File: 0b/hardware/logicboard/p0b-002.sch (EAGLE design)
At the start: 30 parts, among them IC1 7404D, IC4 LTC485S, IC5 LTC485S, J0 DC5V, J7 DIN5, J9 DIN5, X7 NELTRON-7810-XPXC

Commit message: Added Direct-5V resistor pattern.
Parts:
- added R0: Inf, rcl:R-EU_M2012
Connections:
- net V+: now also R0.1
- net VCC: now also R0.2
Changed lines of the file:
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@@
 <part name="S1" library="switch-dil" library_urn="urn:adsk.eagle:library:375" deviceset="DIP04YL" device="" package3d_urn="urn:adsk.eagle:package:27255/2" value="MIDIPHANTOM"/>
 <part name="SUPPLY9" library="supply2" library_urn="urn:adsk.eagle:library:372" deviceset="GND" device=""/>
+<part name="R0" library="rcl" library_urn="urn:adsk.eagle:library:334" deviceset="R-EU_" device="M2012" package3d_urn="urn:adsk.eagle:package:23561/2" value="Inf"/>
 </parts>
 <sheets>
@@
 <instance part="SUPPLY9" gate="GND" x="83.82" y="86.36" smashed="yes">
 <attribute name="VALUE" x="86.995" y="83.185" size="1.778" layer="96"/>
+</instance>
+<instance part="R0" gate="G$1" x="63.5" y="162.56" smashed="yes">
+<attribute name="NAME" x="59.69" y="164.0586" size="1.778" layer="95"/>
+<attribute name="VALUE" x="59.69" y="159.258" size="1.778" layer="96"/>
 </instance>
 </instances>
@@
 <wire x1="66.04" y1="154.94" x2="76.2" y2="154.94" width="0.1524" layer="91"/>
 <wire x1="76.2" y1="154.94" x2="76.2" y2="149.86" width="0.1524" layer="91"/>
+<pinref part="R0" gate="G$1" pin="2"/>
+<wire x1="68.58" y1="162.56" x2="76.2" y2="162.56" width="0.1524" layer="91"/>
+<wire x1="76.2" y1="162.56" x2="76.2" y2="154.94" width="0.1524" layer="91"/>
+<junction x="76.2" y="154.94"/>
 </segment>
 </net>
@@
 <label x="76.2" y="96.52" size="1.778" layer="95"/>
 <label x="76.2" y="91.44" size="1.778" layer="95"/>
-</segment>
-</net>
+<pinref part="R0" gate="G$1" pin="1"/>
+<wire x1="58.42" y1="162.56" x2="50.8" y2="162.56" width="0.1524" layer="91"/>
+<wire x1="50.8" y1="162.56" x2="50.8" y2="154.94" width="0.1524" layer="91"/>
+<junction x="50.8" y="154.94"/>
+</segment>
+</net>

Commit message: Pinhead.
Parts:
- removed R0: Inf, rcl:R-EU_M2012
- added JP1: (no value), pinhead:PINHD-1X2
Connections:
- net V+: now also JP1.1; no longer R0.1
- net VCC: now also JP1.2; no longer R0.2
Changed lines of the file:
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@@
 <part name="S1" library="switch-dil" library_urn="urn:adsk.eagle:library:375" deviceset="DIP04YL" device="" package3d_urn="urn:adsk.eagle:package:27255/2" value="MIDIPHANTOM"/>
 <part name="SUPPLY9" library="supply2" library_urn="urn:adsk.eagle:library:372" deviceset="GND" device=""/>
-<part name="R0" library="rcl" library_urn="urn:adsk.eagle:library:334" deviceset="R-EU_" device="M2012" package3d_urn="urn:adsk.eagle:package:23561/2" value="Inf"/>
+<part name="JP1" library="pinhead" library_urn="urn:adsk.eagle:library:325" deviceset="PINHD-1X2" device="" package3d_urn="urn:adsk.eagle:package:22435/2"/>
 </parts>
 <sheets>
@@
 <attribute name="VALUE" x="86.995" y="83.185" size="1.778" layer="96"/>
 </instance>
-<instance part="R0" gate="G$1" x="63.5" y="162.56" smashed="yes">
-<attribute name="NAME" x="59.69" y="164.0586" size="1.778" layer="95"/>
-<attribute name="VALUE" x="59.69" y="159.258" size="1.778" layer="96"/>
+<instance part="JP1" gate="G$1" x="63.5" y="165.1" smashed="yes" rot="R90">
+<attribute name="NAME" x="57.785" y="158.75" size="1.778" layer="95" rot="R90"/>
+<attribute name="VALUE" x="68.58" y="158.75" size="1.778" layer="96" rot="R90"/>
 </instance>
 </instances>
@@
 <wire x1="66.04" y1="154.94" x2="76.2" y2="154.94" width="0.1524" layer="91"/>
 <wire x1="76.2" y1="154.94" x2="76.2" y2="149.86" width="0.1524" layer="91"/>
-<pinref part="R0" gate="G$1" pin="2"/>
-<wire x1="68.58" y1="162.56" x2="76.2" y2="162.56" width="0.1524" layer="91"/>
-<wire x1="76.2" y1="162.56" x2="76.2" y2="154.94" width="0.1524" layer="91"/>
+<wire x1="76.2" y1="160.02" x2="76.2" y2="154.94" width="0.1524" layer="91"/>
 <junction x="76.2" y="154.94"/>
+<pinref part="JP1" gate="G$1" pin="2"/>
+<wire x1="63.5" y1="162.56" x2="63.5" y2="160.02" width="0.1524" layer="91"/>
+<wire x1="63.5" y1="160.02" x2="76.2" y2="160.02" width="0.1524" layer="91"/>
 </segment>
 </net>
@@
 <label x="76.2" y="96.52" size="1.778" layer="95"/>
 <label x="76.2" y="91.44" size="1.778" layer="95"/>
-<pinref part="R0" gate="G$1" pin="1"/>
-<wire x1="58.42" y1="162.56" x2="50.8" y2="162.56" width="0.1524" layer="91"/>
-<wire x1="50.8" y1="162.56" x2="50.8" y2="154.94" width="0.1524" layer="91"/>
+<wire x1="50.8" y1="160.02" x2="50.8" y2="154.94" width="0.1524" layer="91"/>
 <junction x="50.8" y="154.94"/>
-</segment>
-</net>
+<wire x1="50.8" y1="160.02" x2="60.96" y2="160.02" width="0.1524" layer="91"/>
+<pinref part="JP1" gate="G$1" pin="1"/>
+<wire x1="60.96" y1="160.02" x2="60.96" y2="162.56" width="0.1524" layer="91"/>
+</segment>
+</net>

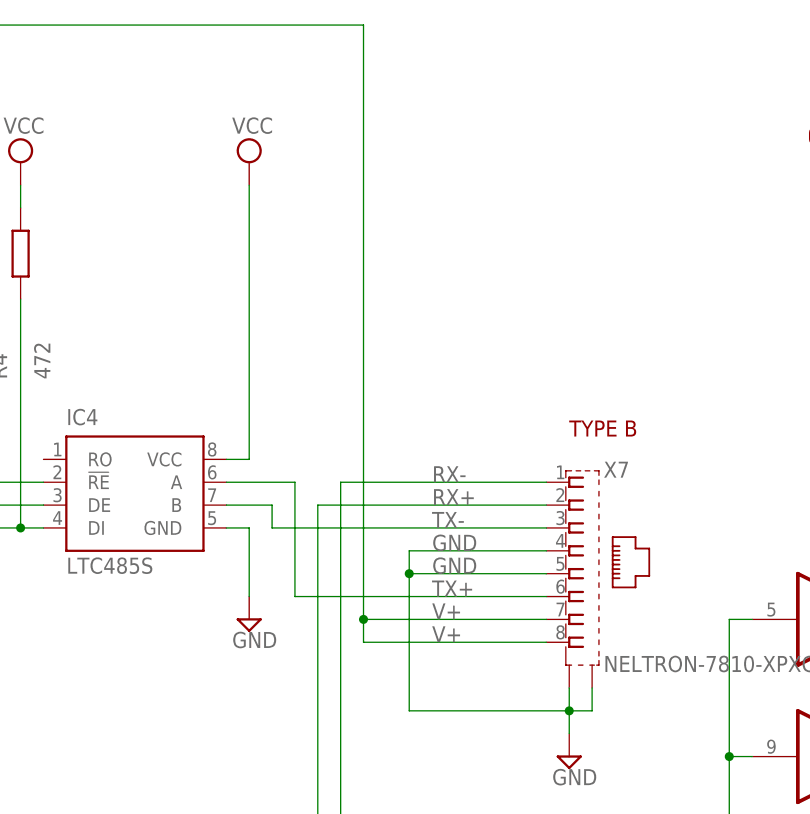
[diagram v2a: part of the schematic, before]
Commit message: Added PoE R.
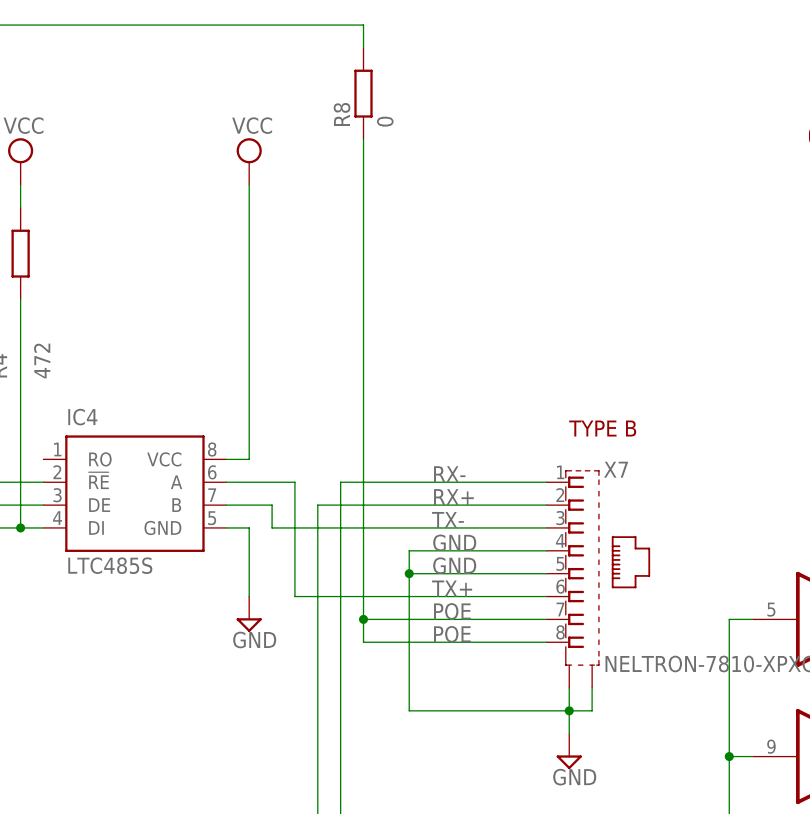
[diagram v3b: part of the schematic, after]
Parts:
- added R8: 0, rcl:R-EU_M2012
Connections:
- new net POE: R8.1, X7.7, X7.8
- net V+: now also R8.2; no longer X7.7, X7.8
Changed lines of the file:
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@@
 <part name="SUPPLY9" library="supply2" library_urn="urn:adsk.eagle:library:372" deviceset="GND" device=""/>
 <part name="JP1" library="pinhead" library_urn="urn:adsk.eagle:library:325" deviceset="PINHD-1X2" device="" package3d_urn="urn:adsk.eagle:package:22435/2"/>
+<part name="R8" library="rcl" library_urn="urn:adsk.eagle:library:334" deviceset="R-EU_" device="M2012" package3d_urn="urn:adsk.eagle:package:23561/2" value="0"/>
 </parts>
 <sheets>
@@
 <attribute name="NAME" x="57.785" y="158.75" size="1.778" layer="95" rot="R90"/>
 <attribute name="VALUE" x="68.58" y="158.75" size="1.778" layer="96" rot="R90"/>
+</instance>
+<instance part="R8" gate="G$1" x="180.34" y="162.56" smashed="yes" rot="R90">
+<attribute name="NAME" x="178.8414" y="158.75" size="1.778" layer="95" rot="R90"/>
+<attribute name="VALUE" x="183.642" y="158.75" size="1.778" layer="96" rot="R90"/>
 </instance>
 </instances>
@@
 <label x="30.48" y="149.86" size="1.778" layer="95"/>
 <wire x1="38.1" y1="149.86" x2="38.1" y2="170.18" width="0.1524" layer="91"/>
-<pinref part="X7" gate="G$1" pin="7"/>
-<wire x1="200.66" y1="104.14" x2="180.34" y2="104.14" width="0.1524" layer="91"/>
-<pinref part="X7" gate="G$1" pin="8"/>
-<wire x1="200.66" y1="101.6" x2="180.34" y2="101.6" width="0.1524" layer="91"/>
-<wire x1="180.34" y1="101.6" x2="180.34" y2="104.14" width="0.1524" layer="91"/>
-<junction x="180.34" y="104.14"/>
 <wire x1="38.1" y1="170.18" x2="101.6" y2="170.18" width="0.1524" layer="91"/>
 <wire x1="101.6" y1="170.18" x2="180.34" y2="170.18" width="0.1524" layer="91"/>
-<wire x1="180.34" y1="170.18" x2="180.34" y2="104.14" width="0.1524" layer="91"/>
 <pinref part="S1" gate="1" pin="7"/>
 <wire x1="76.2" y1="96.52" x2="101.6" y2="96.52" width="0.1524" layer="91"/>
@@
 <junction x="101.6" y="96.52"/>
 <junction x="101.6" y="170.18"/>
-<label x="187.96" y="104.14" size="1.778" layer="95"/>
-<label x="187.96" y="101.6" size="1.778" layer="95"/>
 <label x="76.2" y="96.52" size="1.778" layer="95"/>
 <label x="76.2" y="91.44" size="1.778" layer="95"/>
@@
 <pinref part="JP1" gate="G$1" pin="1"/>
 <wire x1="60.96" y1="160.02" x2="60.96" y2="162.56" width="0.1524" layer="91"/>
+<pinref part="R8" gate="G$1" pin="2"/>
+<wire x1="180.34" y1="170.18" x2="180.34" y2="167.64" width="0.1524" layer="91"/>
 </segment>
 </net>
@@
 </segment>
 </net>
+<net name="POE" class="1">
+<segment>
+<pinref part="X7" gate="G$1" pin="7"/>
+<wire x1="200.66" y1="104.14" x2="180.34" y2="104.14" width="0.1524" layer="91"/>
+<pinref part="X7" gate="G$1" pin="8"/>
+<wire x1="200.66" y1="101.6" x2="180.34" y2="101.6" width="0.1524" layer="91"/>
+<wire x1="180.34" y1="101.6" x2="180.34" y2="104.14" width="0.1524" layer="91"/>
+<label x="187.96" y="104.14" size="1.778" layer="95"/>
+<label x="187.96" y="101.6" size="1.778" layer="95"/>
+<pinref part="R8" gate="G$1" pin="1"/>
+<wire x1="180.34" y1="157.48" x2="180.34" y2="104.14" width="0.1524" layer="91"/>
+<junction x="180.34" y="104.14"/>
+</segment>
+</net>

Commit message: Pinhead.
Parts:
- added JP2: (no value), pinhead:PINHD-1X2
- R8: value 0 -> 20
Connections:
- new net POERAW: JP2.1, R8.1
- net POE: now also JP2.2; no longer R8.1
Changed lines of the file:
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@@
 <part name="SUPPLY9" library="supply2" library_urn="urn:adsk.eagle:library:372" deviceset="GND" device=""/>
 <part name="JP1" library="pinhead" library_urn="urn:adsk.eagle:library:325" deviceset="PINHD-1X2" device="" package3d_urn="urn:adsk.eagle:package:22435/2"/>
-<part name="R8" library="rcl" library_urn="urn:adsk.eagle:library:334" deviceset="R-EU_" device="M2012" package3d_urn="urn:adsk.eagle:package:23561/2" value="0"/>
+<part name="R8" library="rcl" library_urn="urn:adsk.eagle:library:334" deviceset="R-EU_" device="M2012" package3d_urn="urn:adsk.eagle:package:23561/2" value="20"/>
+<part name="JP2" library="pinhead" library_urn="urn:adsk.eagle:library:325" deviceset="PINHD-1X2" device="" package3d_urn="urn:adsk.eagle:package:22435/2"/>
 </parts>
 <sheets>
@@
 <attribute name="NAME" x="178.8414" y="158.75" size="1.778" layer="95" rot="R90"/>
 <attribute name="VALUE" x="183.642" y="158.75" size="1.778" layer="96" rot="R90"/>
+</instance>
+<instance part="JP2" gate="G$1" x="185.42" y="144.78" smashed="yes">
+<attribute name="NAME" x="179.07" y="150.495" size="1.778" layer="95"/>
+<attribute name="VALUE" x="179.07" y="139.7" size="1.778" layer="96"/>
 </instance>
 </instances>
@@
 <label x="187.96" y="104.14" size="1.778" layer="95"/>
 <label x="187.96" y="101.6" size="1.778" layer="95"/>
+<pinref part="JP2" gate="G$1" pin="2"/>
+<wire x1="182.88" y1="144.78" x2="180.34" y2="144.78" width="0.1524" layer="91"/>
+<wire x1="180.34" y1="144.78" x2="180.34" y2="104.14" width="0.1524" layer="91"/>
+<junction x="180.34" y="104.14"/>
+</segment>
+</net>
+<net name="POERAW" class="1">
+<segment>
 <pinref part="R8" gate="G$1" pin="1"/>
-<wire x1="180.34" y1="157.48" x2="180.34" y2="104.14" width="0.1524" layer="91"/>
-<junction x="180.34" y="104.14"/>
-</segment>
-</net>
+<wire x1="180.34" y1="157.48" x2="180.34" y2="147.32" width="0.1524" layer="91"/>
+<pinref part="JP2" gate="G$1" pin="1"/>
+<wire x1="180.34" y1="147.32" x2="182.88" y2="147.32" width="0.1524" layer="91"/>
+</segment>
+</net>
